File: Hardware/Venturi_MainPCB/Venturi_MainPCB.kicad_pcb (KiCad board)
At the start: 2 copper layers, 166.1 x 91.4 mm, 72 parts, among them J1 Battery, J2 ESC_PWM, J3 ESC_P, J4 ESC_N, J5 M1, J6 M1, J7 Sensor-PCB, Q1 BSS138, Q2 DMP3013SFV, SW1 POWER_EN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

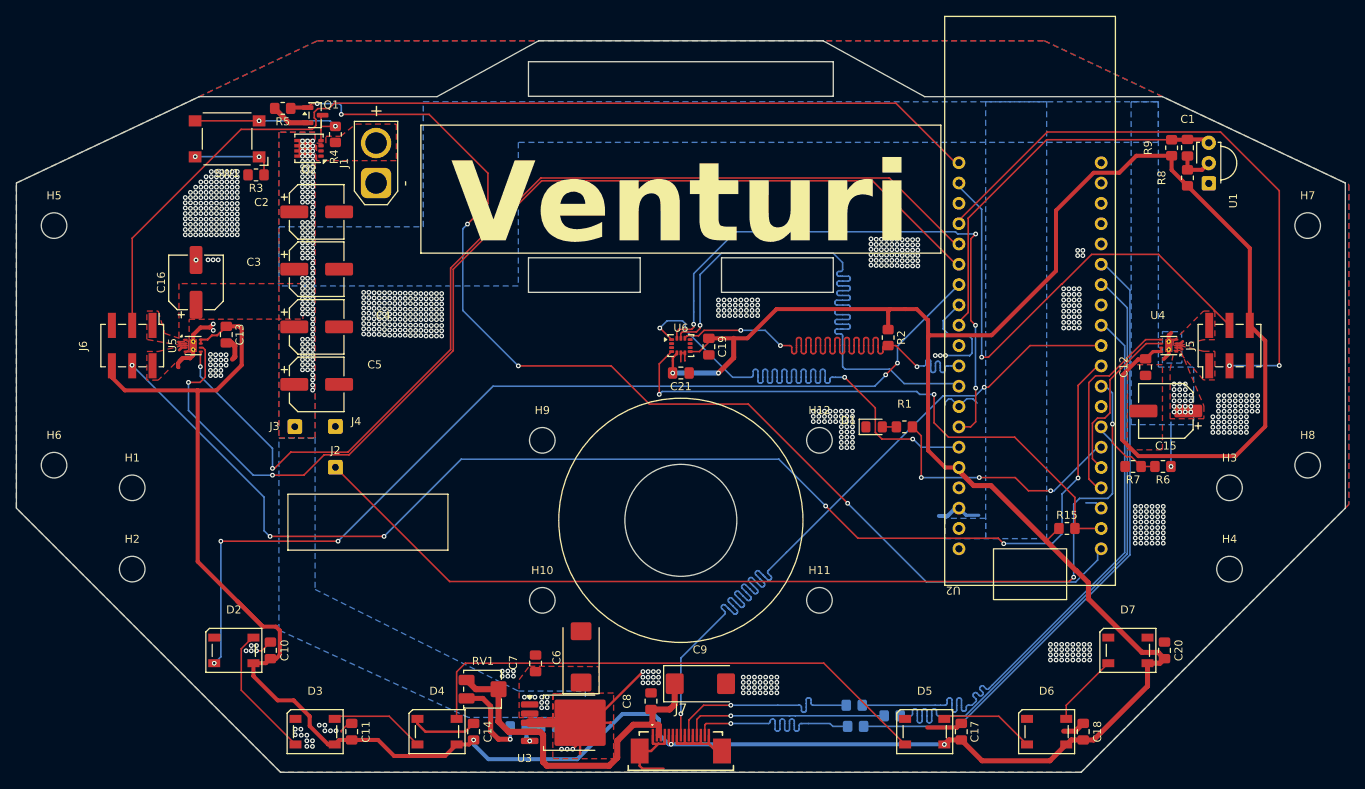
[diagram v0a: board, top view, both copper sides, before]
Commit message: Switched to pure ESP-IDF for the ESP32-P4. Added custom firmware for the onboard ESP32-C6
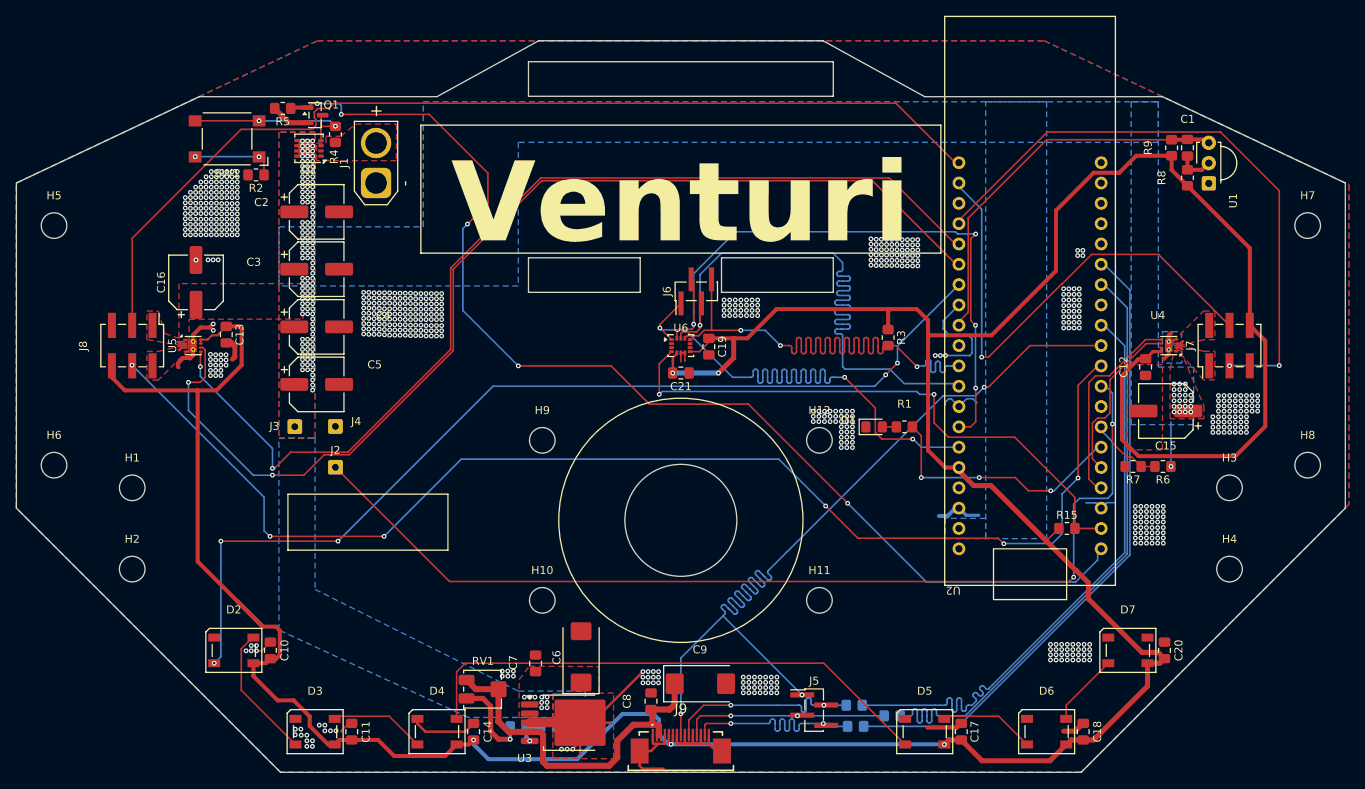
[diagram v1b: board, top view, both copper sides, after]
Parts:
- added J5: SPI_ADC, Connector_PinHeader_1.27mm:PinHeader_1x04_P1.27mm_Vertical_SMD_Pin1Left, F.Cu at (154.5, 134.8)
- added J6: SPI_IMU, Connector_PinHeader_1.27mm:PinHeader_1x04_P1.27mm_Vertical_SMD_Pin1Left, F.Cu at (139.8, 82.5)
- renumbered J5 to J7, J6 to J8, J7 to J9, R3 to R2, R2 to R3
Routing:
- net MISO: track 98.9 -> 112.9 mm, vias 2 -> 3
- net IMU_CS: track 75.0 -> 81.4 mm
- net IMU_MOSI: track 73.8 -> 79.5 mm
- net IMU_MISO: track 72.3 -> 75.3 mm
- net IMU_CLK: track 78.2 -> 81.0 mm
- net GND: track 132.1 -> 134.0 mm, vias 674 -> 670
- net CLK: track 25.6 -> 26.2 mm, vias 1 -> 2
- net CS: track 26.5 -> 26.9 mm, vias 1 -> 2
- net MOSI: track 25.3 -> 25.6 mm, vias 1 -> 2
